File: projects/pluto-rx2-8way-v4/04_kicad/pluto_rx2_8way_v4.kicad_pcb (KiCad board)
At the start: 4 copper layers, 50 x 73 mm, 32 parts

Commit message: Complete RX2 8-way v4 design repairs
Use the RP2040 module, close filtered-rail and control-edge margins, add a real four-layer stackup and routed module keepout, update firmware drive settings, and archive the superseded review findings.
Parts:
- R_S1, R_S2, R_S3, R_S4: value 47Ω -> 100Ω
- moved C_BULK 7.28 mm to (65.8, 82.8), turned to 0 degrees
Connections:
- C_BULK pad 1: 3V3_MOD -> 3V3
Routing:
- net 3V3: track 48.4 -> 57.4 mm
- net SW_V4: track 37.7 -> 43.6 mm, vias 2 -> 3
- net 3V3_MOD: track 5.03 -> 3.03 mm
- net GND: vias 3443 -> 3429
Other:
- board text added: "ANT8 = RX1 TAP"
- board text removed: "ANT8 = RX1 TAP -20.26 dB"

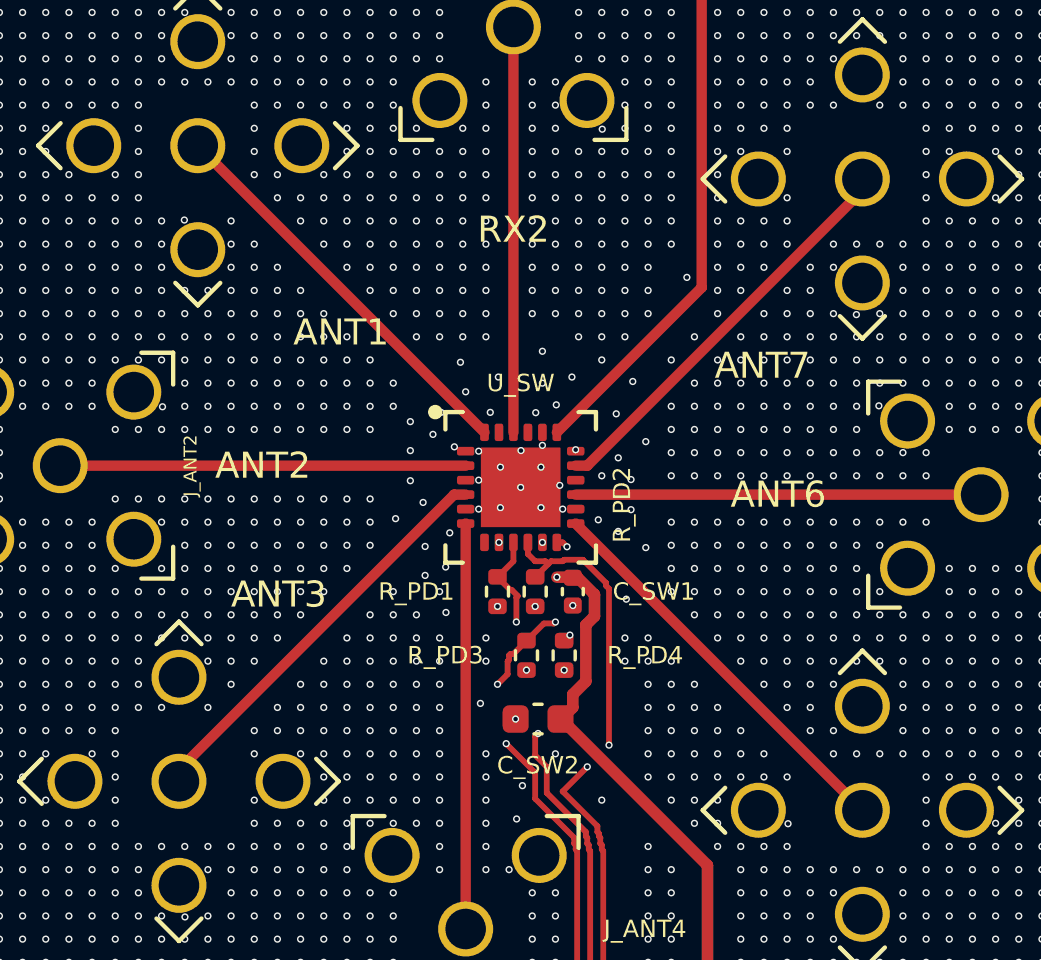
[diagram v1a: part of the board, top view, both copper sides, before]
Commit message: Close RX2 v4 adversarial layout blockers
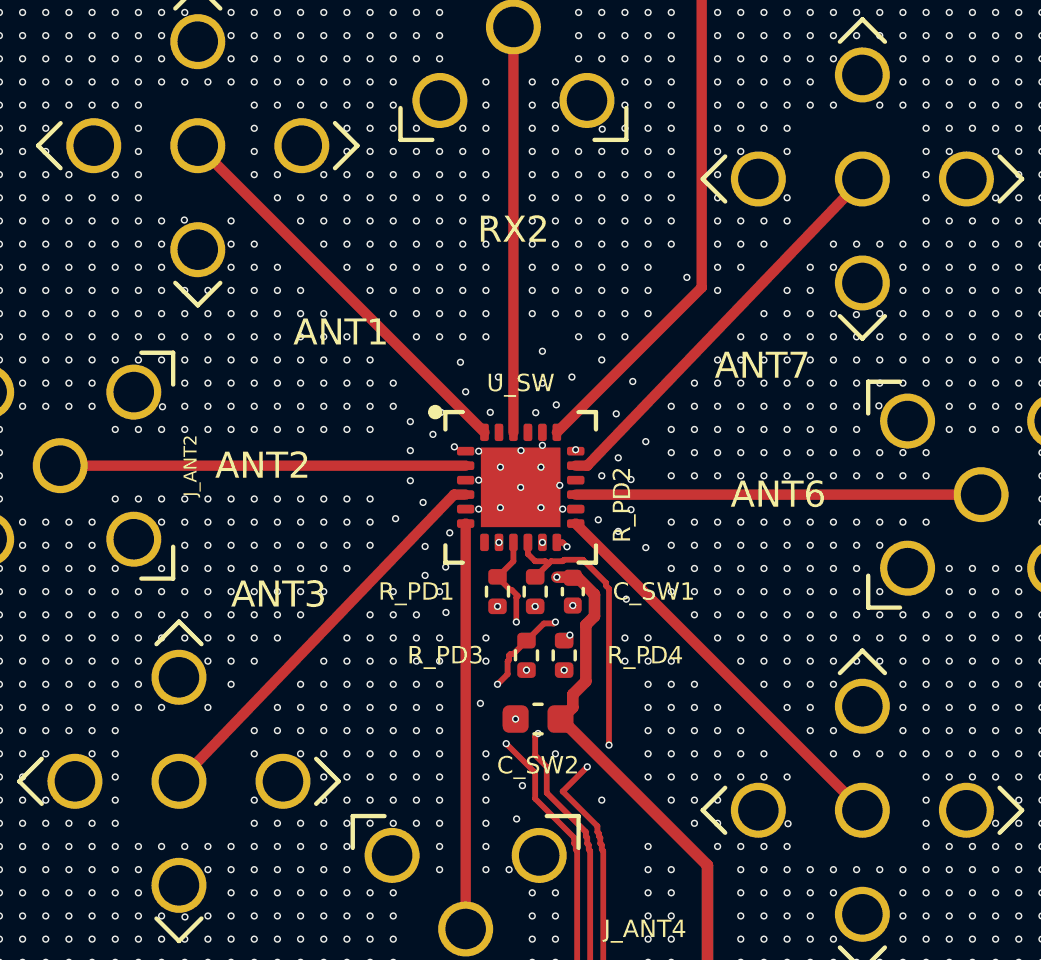
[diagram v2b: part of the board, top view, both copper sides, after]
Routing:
- net GND: vias 3429 -> 3423
